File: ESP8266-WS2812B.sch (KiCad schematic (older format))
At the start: 14 parts

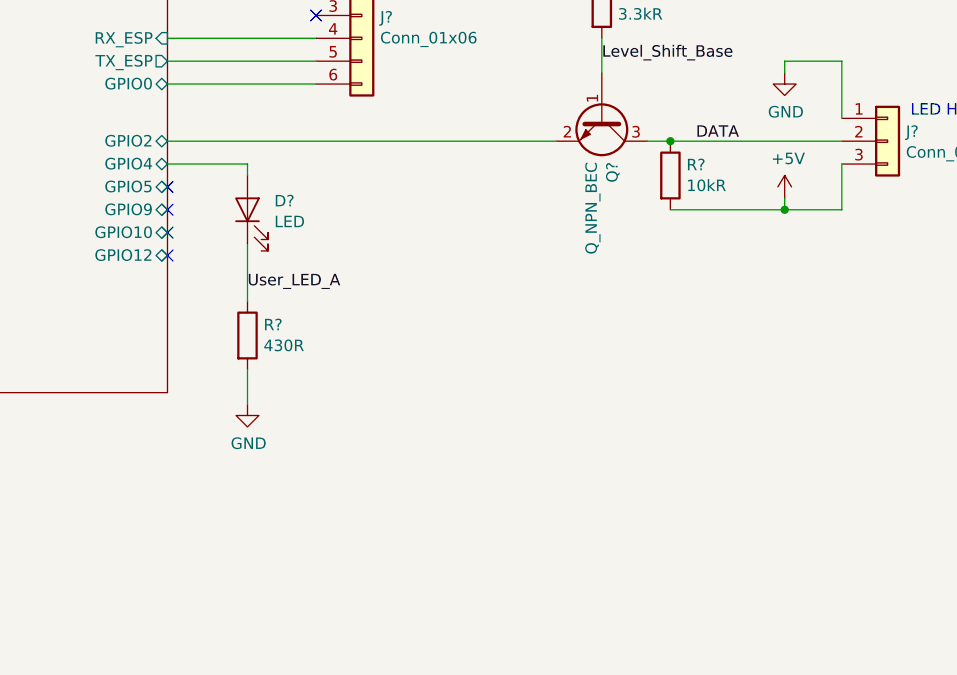
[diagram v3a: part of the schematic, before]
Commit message: Added a user button for general use
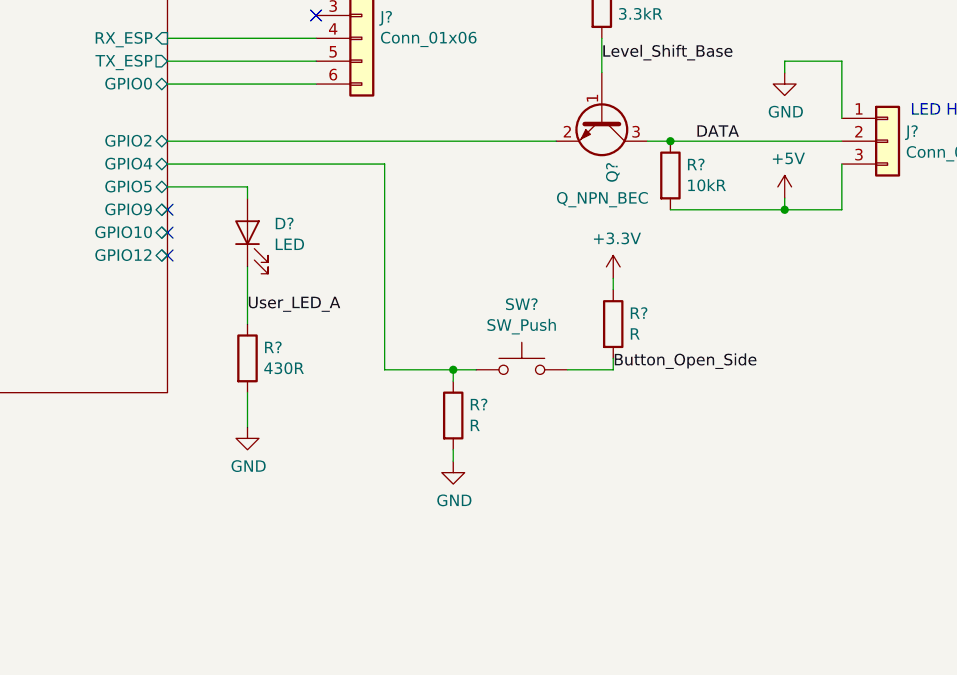
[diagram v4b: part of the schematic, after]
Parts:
- added R? (x2): R, symbol Device:R
- added SW?: SW_Push, symbol Switch:SW_Push
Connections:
- net +3V3: now also R?.1
- net ESP8266/GPIO4: now also R?.1, SW?.1; no longer D?.2 (A)
- net ESP8266/GPIO5: now also D?.2 (A)
- net GND: now also R?.2
- new net Button_Open_Side: R?.2, SW?.2
- no-connect marks 18 -> 17
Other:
- moved on the sheet: D?, R?
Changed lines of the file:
@@
 NoConn ~ 6350 5150
 NoConn ~ 6350 5050
-NoConn ~ 6350 4950
 Text Label 8850 4750 2    50   ~ 0
 DATA
@@
 P 8250 4650
 F 0 "Q?" H 8441 4696 50  0000 L CNN
-F 1 "Q_NPN_BEC" H 8441 4605 50  0000 L CNN
+F 1 "Q_NPN_BEC" V 8600 4450 50  0000 L CNN
 F 2 "" H 8450 4750 50  0001 C CNN
 F 3 "~" H 8250 4650 50  0001 C CNN
@@
 L Device:LED D?
 U 1 1 5BCF56F1
-P 6700 5050
-F 0 "D?" V 6738 4933 50  0000 R CNN
-F 1 "LED" V 6647 4933 50  0000 R CNN
-F 2 "" H 6700 5050 50  0001 C CNN
-F 3 "~" H 6700 5050 50  0001 C CNN
-	1    6700 5050
+P 6700 5150
+F 0 "D?" V 6738 5033 50  0000 R CNN
+F 1 "LED" V 6647 5033 50  0000 R CNN
+F 2 "" H 6700 5150 50  0001 C CNN
+F 3 "~" H 6700 5150 50  0001 C CNN
+	1    6700 5150
 	0    -1   -1   0
 $EndComp
@@
 L Device:R R?
 U 1 1 5BCF56F8
-P 6700 5600
-F 0 "R?" H 6770 5646 50  0000 L CNN
-F 1 "430R" H 6770 5555 50  0000 L CNN
-F 2 "" V 6630 5600 50  0001 C CNN
-F 3 "~" H 6700 5600 50  0001 C CNN
-	1    6700 5600
-	1    0    0    -1
-$EndComp
-Wire Wire Line
-	6700 5200 6700 5450
-Wire Wire Line
-	6700 5900 6700 5750
-Text Label 6700 5400 0    50   ~ 0
+P 6700 5700
+F 0 "R?" H 6770 5746 50  0000 L CNN
+F 1 "430R" H 6770 5655 50  0000 L CNN
+F 2 "" V 6630 5700 50  0001 C CNN
+F 3 "~" H 6700 5700 50  0001 C CNN
+	1    6700 5700
+	1    0    0    -1
+$EndComp
+Wire Wire Line
+	6700 5300 6700 5550
+Wire Wire Line
+	6700 6000 6700 5850
+Text Label 6700 5500 0    50   ~ 0
 User_LED_A
 Wire Wire Line
-	6350 4850 6700 4850
-Wire Wire Line
-	6700 4850 6700 4900
+	6350 4950 6700 4950
+Wire Wire Line
+	6700 4950 6700 5000
 $Comp
 L power:GND #PWR?
 U 1 1 5BCF7B29
-P 6700 5900
-F 0 "#PWR?" H 6700 5650 50  0001 C CNN
-F 1 "GND" H 6705 5727 50  0000 C CNN
-F 2 "" H 6700 5900 50  0001 C CNN
-F 3 "" H 6700 5900 50  0001 C CNN
-	1    6700 5900
+P 6700 6000
+F 0 "#PWR?" H 6700 5750 50  0001 C CNN
+F 1 "GND" H 6705 5827 50  0000 C CNN
+F 2 "" H 6700 6000 50  0001 C CNN
+F 3 "" H 6700 6000 50  0001 C CNN
+	1    6700 6000
 	1    0    0    -1
 $EndComp
@@
 	1    0    0    -1
 $EndComp
+$Comp
+L Switch:SW_Push SW?
+U 1 1 5BDC7808
+P 7900 5750
+F 0 "SW?" H 7900 6035 50  0000 C CNN
+F 1 "SW_Push" H 7900 5944 50  0000 C CNN
+F 2 "" H 7900 5950 50  0001 C CNN
+F 3 "" H 7900 5950 50  0001 C CNN
+	1    7900 5750
+	1    0    0    -1
+$EndComp
+Wire Wire Line
+	7700 5750 7600 5750
+Wire Wire Line
+	7300 4850 6350 4850
+$Comp
+L Device:R R?
+U 1 1 5BDC84DB
+P 7600 5950
+F 0 "R?" H 7670 5996 50  0000 L CNN
+F 1 "R" H 7670 5905 50  0000 L CNN
+F 2 "" V 7530 5950 50  0001 C CNN
+F 3 "~" H 7600 5950 50  0001 C CNN
+	1    7600 5950
+	1    0    0    -1
+$EndComp
+Wire Wire Line
+	7600 5750 7600 5800
+Connection ~ 7600 5750
+Wire Wire Line
+	7600 5750 7300 5750
+$Comp
+L power:GND #PWR?
+U 1 1 5BDC91C9
+P 7600 6150
+F 0 "#PWR?" H 7600 5900 50  0001 C CNN
+F 1 "GND" H 7605 5977 50  0000 C CNN
+F 2 "" H 7600 6150 50  0001 C CNN
+F 3 "" H 7600 6150 50  0001 C CNN
+	1    7600 6150
+	1    0    0    -1
+$EndComp
+Wire Wire Line
+	7600 6150 7600 6100
+$Comp
+L Device:R R?
+U 1 1 5BDCA73F
+P 8300 5550
+F 0 "R?" H 8370 5596 50  0000 L CNN
+F 1 "R" H 8370 5505 50  0000 L CNN
+F 2 "" V 8230 5550 50  0001 C CNN
+F 3 "~" H 8300 5550 50  0001 C CNN
+	1    8300 5550
+	1    0    0    -1
+$EndComp
+$Comp
+L ESP8266-WS2812B-cache:+3.3V #PWR?
+U 1 1 5BDCAED8
+P 8300 5350
+F 0 "#PWR?" H 8300 5200 50  0001 C CNN
+F 1 "+3.3V" H 8315 5523 50  0000 C CNN
+F 2 "" H 8300 5350 50  0001 C CNN
+F 3 "" H 8300 5350 50  0001 C CNN
+	1    8300 5350
+	1    0    0    -1
+$EndComp
+Wire Wire Line
+	8300 5350 8300 5400
+Wire Wire Line
+	8100 5750 8300 5750
+Wire Wire Line
+	8300 5750 8300 5700
+Text Label 8300 5750 0    50   ~ 0
+Button_Open_Side
+Wire Wire Line
+	7300 4850 7300 5750
 $EndSCHEMATC

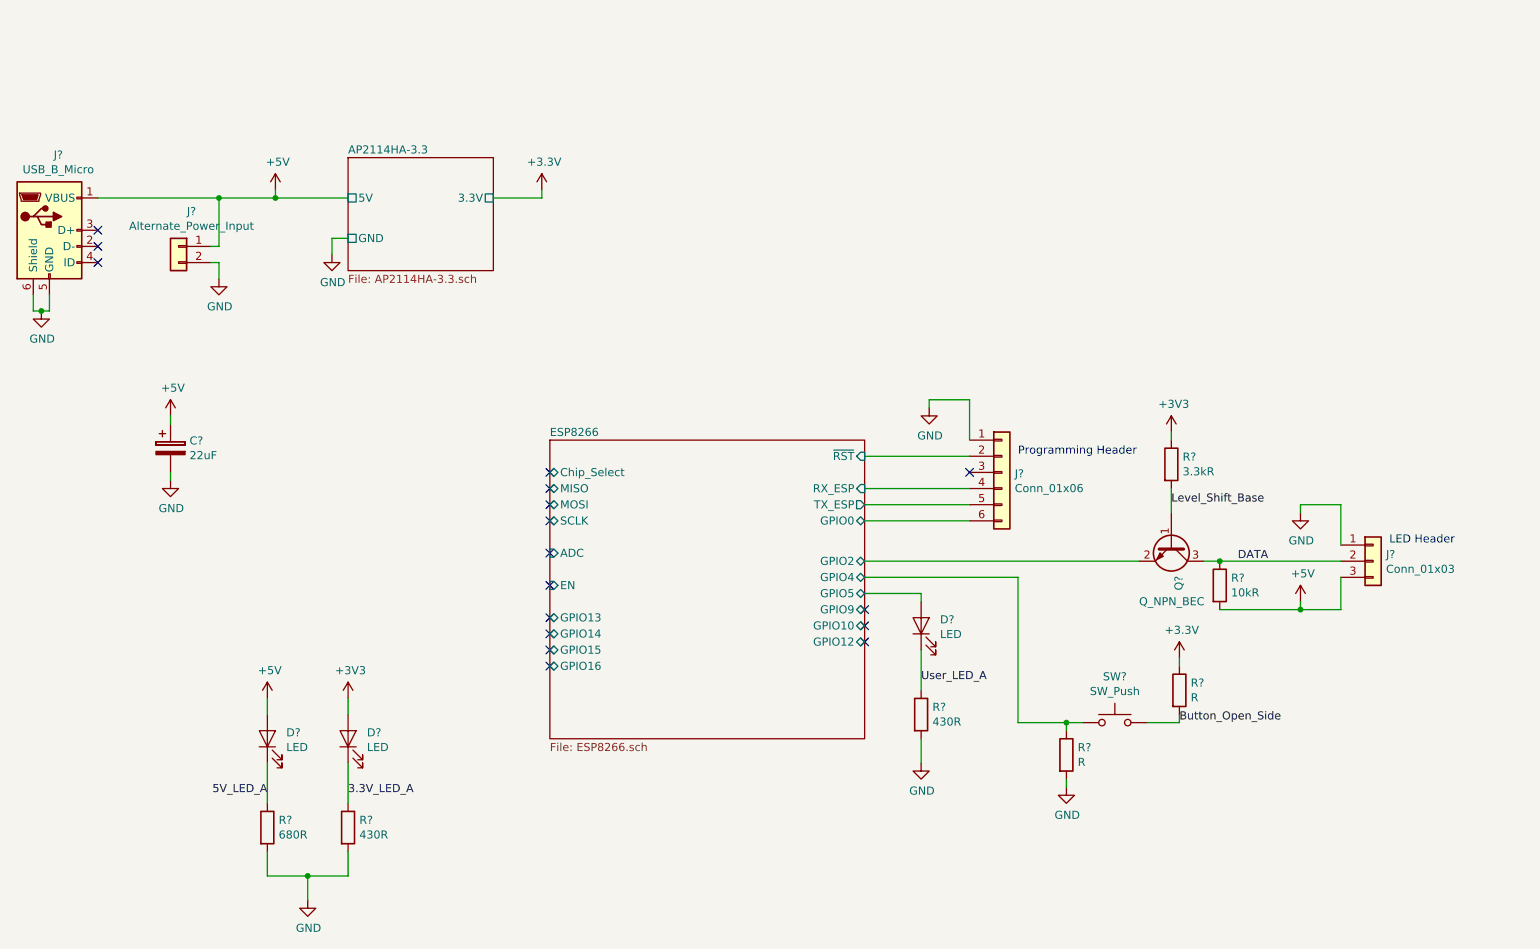
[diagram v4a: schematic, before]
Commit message: Annotated schematic and added footprints.
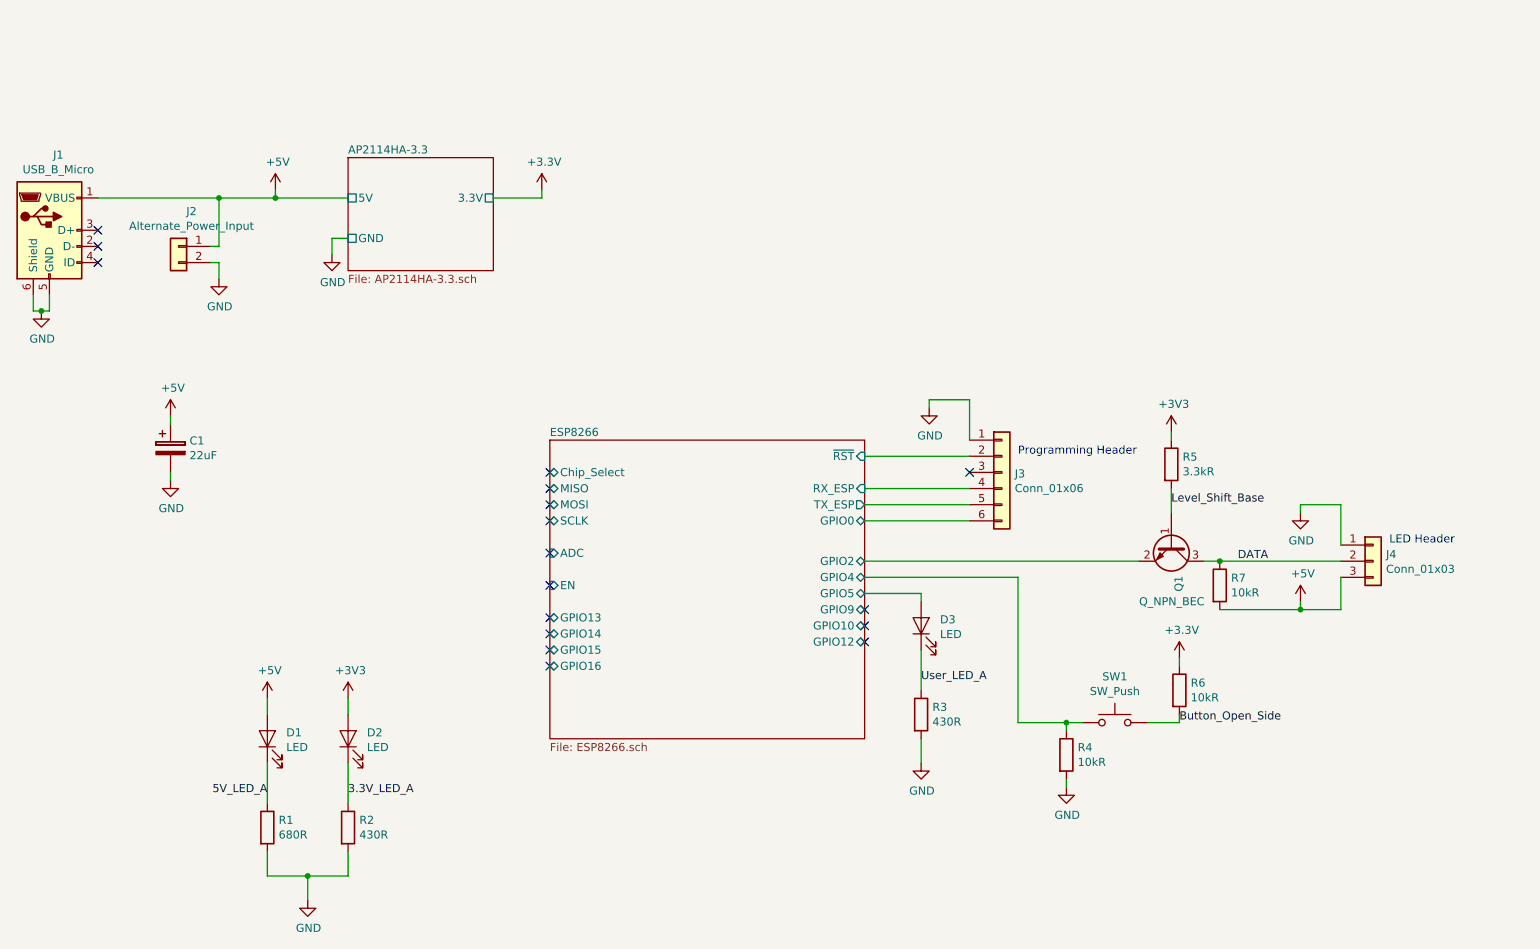
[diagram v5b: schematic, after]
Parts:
- C1: renamed from C?; footprint (none) -> Capacitors_THT:CP_Radial_D5.0mm_P2.00mm
- D1, D2, D3: renamed from D?; footprint (none) -> LEDs:LED_0805
- J1: renamed from J?; footprint (none) -> Connectors:USB_Micro-B
- J2: renamed from J?; footprint (none) -> Connectors_Molex:Molex_KK-6410-02_02x2.54mm_Straight
- J3: renamed from J?; footprint (none) -> Pin_Headers:Pin_Header_Angled_1x06_Pitch2.54mm
- J4: renamed from J?; footprint (none) -> Connectors_Molex:Molex_KK-6410-03_03x2.54mm_Straight
- Q1: renamed from Q?; footprint (none) -> TO_SOT_Packages_SMD:SOT-23
- R1, R2, R3: renamed from R?; footprint (none) -> Resistors_SMD:R_0805
- R4, R6: renamed from R?; value R -> 10kR; footprint (none) -> Resistors_SMD:R_0603
- R5, R7: renamed from R?; footprint (none) -> Resistors_SMD:R_0603
- SW1: renamed from SW?; footprint (none) -> Buttons_Switches_THT:SW_PUSH-12mm

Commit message: Fixed library symbol for the 3.3V regulator. Also added correct footprint path for the ESP-12E.
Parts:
- J3: footprint Pin_Headers:Pin_Header_Angled_1x06_Pitch2.54mm -> Pin_Headers:Pin_Header_Straight_1x06_Pitch2.54mm
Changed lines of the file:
@@
 F 0 "J3" H 7280 4192 50  0000 L CNN
 F 1 "Conn_01x06" H 7280 4101 50  0000 L CNN
-F 2 "Pin_Headers:Pin_Header_Angled_1x06_Pitch2.54mm" H 7200 4200 50  0001 C CNN
+F 2 "Pin_Headers:Pin_Header_Straight_1x06_Pitch2.54mm" H 7200 4200 50  0001 C CNN
 F 3 "~" H 7200 4200 50  0001 C CNN
 	1    7200 4200
